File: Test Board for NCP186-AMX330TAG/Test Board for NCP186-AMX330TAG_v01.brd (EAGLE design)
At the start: 11 x 9.3 mm, 7 parts

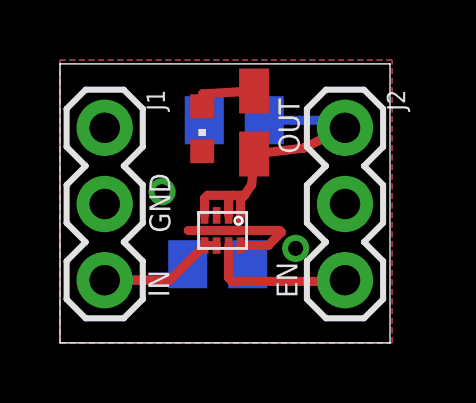
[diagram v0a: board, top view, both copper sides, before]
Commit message: Updated NCP part
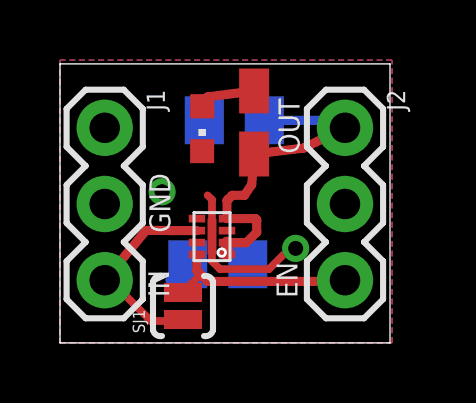
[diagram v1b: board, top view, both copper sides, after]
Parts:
- added SJ1: SOLDERJUMPERNO, SparkFun-Retired:SJ_2S-NO
- moved U$1 1.70 mm to (5.67, 2.74), turned to 90 degrees
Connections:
- net EN: now also J1.3, SJ1.1; no longer J2.3
- net IIN: now also J2.3, SJ1.2; no longer J1.3
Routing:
- net EN: track 5.02 -> 7.05 mm
- net GND: track 4.19 -> 5.43 mm
- net OUT: track 10.8 -> 11.7 mm
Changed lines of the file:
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@@
 <elements>
 <element name="C1" library="resistor" package="C0805K" value="" x="5.81" y="7.42" rot="MR0"/>
-<element name="U$1" library="Ladvien_Eagle_Parts" package="XDFN8" value="NCP186-AMX330TAG" x="6.22" y="4.35" smashed="yes" rot="R180"/>
 <element name="C2" library="resistor" package="C0805K" value="" x="5.26" y="2.62" rot="MR180"/>
 <element name="J1" library="SparkFun-Connectors" package="1X03" value="" x="1.49" y="7.17" rot="R270"/>
@@
 <attribute name="VALUE" x="9.01184375" y="6.71238125" size="1.27" layer="27" rot="R90"/>
 </element>
+<element name="U$1" library="Ladvien_Eagle_Parts" package="XDFN8" value="NCP186-AMX330TAG" x="5.6672625" y="2.7424625" rot="R90"/>
+<element name="SJ1" library="SparkFun-Retired" package="SJ_2S-NO" value="SOLDERJUMPERNO" x="4.1" y="1.23" rot="R90"/>
 </elements>
 <signals>
 <signal name="IIN">
-<contactref element="J1" pad="3"/>
 <contactref element="C2" pad="1"/>
-<contactref element="U$1" pad="8"/>
-<contactref element="U$1" pad="7"/>
-<wire x1="1.49" y1="2.09" x2="3.6625" y2="2.09" width="0.3048" layer="1"/>
-<wire x1="3.6625" y1="2.09" x2="4.82" y2="3.2475" width="0.3048" layer="1"/>
-<wire x1="4.82" y1="3.2475" x2="5.22" y2="3.2475" width="0.3048" layer="1"/>
 <wire x1="4.26" y1="2.62" x2="4.1925" y2="2.62" width="0.3048" layer="16"/>
 <wire x1="4.1925" y1="2.62" x2="3.6625" y2="2.09" width="0.3048" layer="16"/>
-<wire x1="3.6625" y1="2.09" x2="1.49" y2="2.09" width="0.3048" layer="16"/>
+<contactref element="U$1" pad="7" route="any" routetag="G$1.IN"/>
+<contactref element="U$1" pad="8" route="any" routetag="G$1.IN"/>
+<contactref element="J2" pad="3"/>
+<wire x1="4.5647625" y1="2.9424625" x2="4.5647625" y2="2.4052375" width="0.3048" layer="1"/>
+<wire x1="4.5647625" y1="2.4052375" x2="4.68653125" y2="2.28346875" width="0.3048" layer="1"/>
+<wire x1="4.68653125" y1="2.28346875" x2="4.92" y2="2.05" width="0.3048" layer="1"/>
+<wire x1="4.92" y1="2.05" x2="9.46" y2="2.05" width="0.3048" layer="1"/>
+<wire x1="9.46" y1="2.05" x2="9.5" y2="2.09" width="0.4064" layer="1"/>
+<contactref element="SJ1" pad="2"/>
+<wire x1="4.1" y1="1.68" x2="4.1" y2="1.6969375" width="0.254" layer="1"/>
+<wire x1="4.1" y1="1.6969375" x2="4.68653125" y2="2.28346875" width="0.254" layer="1"/>
+<wire x1="4.5647625" y1="2.4052375" x2="4.26" y2="2.62" width="0" layer="19" extent="1-16"/>
 </signal>
 <signal name="GND">
 <contactref element="J1" pad="2"/>
-<contactref element="U$1" pad="PAD"/>
-<contactref element="U$1" pad="5"/>
 <contactref element="C2" pad="2"/>
 <contactref element="C1" pad="2"/>
@@
 <vertex x="11.07" y="9.43"/>
 </polygon>
-<wire x1="5.42" y1="3.75" x2="7.32" y2="3.75" width="0.3048" layer="1"/>
-<wire x1="7.32" y1="3.75" x2="7.38" y2="3.69" width="0.3048" layer="1"/>
-<wire x1="6.02" y1="3.2475" x2="6.9375" y2="3.2475" width="0.3048" layer="1"/>
-<wire x1="6.9375" y1="3.2475" x2="7.38" y2="3.69" width="0.3048" layer="1"/>
 <via x="3.402915625" y="5.03813125" extent="1-16" drill="0.5"/>
 <via x="7.855496875" y="3.1503875" extent="1-16" drill="0.5"/>
-<wire x1="4.935915625" y1="3.745275" x2="4.27164375" y2="3.745275" width="0.3048" layer="1"/>
+<contactref element="U$1" pad="PAD"/>
+<contactref element="U$1" pad="5"/>
+<wire x1="5.0672625" y1="3.5424625" x2="5.0672625" y2="4.7727375" width="0.254" layer="1"/>
+<wire x1="5.0672625" y1="4.7727375" x2="4.92" y2="4.92" width="0.254" layer="1"/>
+<wire x1="5.0672625" y1="3.5424625" x2="5.0672625" y2="2.7227375" width="0.254" layer="1"/>
+<wire x1="5.0672625" y1="2.7227375" x2="5.33" y2="2.46" width="0.254" layer="1"/>
+<wire x1="5.33" y1="2.46" x2="6.97" y2="2.46" width="0.254" layer="1"/>
+<wire x1="6.97" y1="2.46" x2="7.79" y2="3.28" width="0.254" layer="1"/>
+<wire x1="5.0672625" y1="3.5424625" x2="4.5647625" y2="4.1424625" width="0" layer="19" extent="1-1"/>
 </signal>
 <signal name="OUT">
-<contactref element="U$1" pad="4"/>
-<contactref element="U$1" pad="1"/>
-<contactref element="U$1" pad="2"/>
 <contactref element="J2" pad="1"/>
 <contactref element="C1" pad="1"/>
@@
 <wire x1="6.39215" y1="5.280259375" x2="6.15" y2="4.92" width="0.3048" layer="1"/>
 <wire x1="6.15" y1="4.92" x2="5.74" y2="4.92" width="0.3048" layer="1"/>
-<wire x1="5.74" y1="4.92" x2="4.92" y2="4.92" width="0.3048" layer="1"/>
-<wire x1="4.82" y1="4.25" x2="4.82" y2="4.82" width="0.3048" layer="1"/>
-<wire x1="4.82" y1="4.82" x2="4.92" y2="4.92" width="0.3048" layer="1"/>
-<wire x1="5.62" y1="4.25" x2="5.62" y2="4.8" width="0.3048" layer="1"/>
 <wire x1="5.62" y1="4.8" x2="5.74" y2="4.92" width="0.3048" layer="1"/>
-<wire x1="6.02" y1="4.25" x2="6.02" y2="4.79" width="0.3048" layer="1"/>
-<wire x1="6.02" y1="4.79" x2="6.15" y2="4.92" width="0.3048" layer="1"/>
 <wire x1="6.81" y1="7.42" x2="9.25" y2="7.42" width="0.3048" layer="16"/>
 <wire x1="9.25" y1="7.42" x2="9.5" y2="7.17" width="0.3048" layer="16"/>
+<contactref element="U$1" pad="4"/>
+<contactref element="U$1" pad="1"/>
+<contactref element="U$1" pad="2"/>
+<wire x1="5.5672625" y1="2.9424625" x2="5.5672625" y2="3.3424625" width="0.4064" layer="1"/>
+<wire x1="5.5672625" y1="3.3424625" x2="6.2124625" y2="3.3424625" width="0.3048" layer="1"/>
+<wire x1="6.2124625" y1="3.3424625" x2="6.56" y2="3.69" width="0.3048" layer="1"/>
+<wire x1="5.5672625" y1="4.1424625" x2="6.5175375" y2="4.1424625" width="0.3048" layer="1"/>
+<wire x1="6.5175375" y1="4.1424625" x2="6.56" y2="4.1" width="0.3048" layer="1"/>
+<wire x1="6.56" y1="4.1" x2="6.56" y2="3.69" width="0.3048" layer="1"/>
+<wire x1="5.5672625" y1="4.1424625" x2="5.5672625" y2="4.7472625" width="0.3048" layer="1"/>
+<wire x1="5.5672625" y1="4.7472625" x2="5.62" y2="4.8" width="0.3048" layer="1"/>
 </signal>
 <signal name="EN">
 <contactref element="U$1" pad="6"/>
-<contactref element="J2" pad="3"/>
-<wire x1="5.62" y1="3.2475" x2="5.62" y2="2.17" width="0.3048" layer="1"/>
-<wire x1="5.62" y1="2.17" x2="5.74" y2="2.05" width="0.3048" layer="1"/>
-<wire x1="5.74" y1="2.05" x2="9.46" y2="2.05" width="0.3048" layer="1"/>
-<wire x1="9.46" y1="2.05" x2="9.5" y2="2.09" width="0.3048" layer="1"/>
+<contactref element="J1" pad="3"/>
+<wire x1="4.5647625" y1="3.7424625" x2="3.7424625" y2="3.7424625" width="0.3048" layer="1"/>
+<wire x1="3.7424625" y1="3.7424625" x2="3.46725625" y2="3.74861875" width="0.3048" layer="1"/>
+<wire x1="3.46725625" y1="3.74861875" x2="2.86725625" y2="3.74861875" width="0.3048" layer="1"/>
+<wire x1="2.86725625" y1="3.74861875" x2="1.49" y2="2.09" width="0.3048" layer="1"/>
+<contactref element="SJ1" pad="1"/>
+<wire x1="1.49" y1="2.09" x2="1.672553125" y2="2.09" width="0.254" layer="1"/>
+<wire x1="1.672553125" y1="2.09" x2="3.032228125" y2="0.730325" width="0.254" layer="1"/>
+<wire x1="3.032228125" y1="0.730325" x2="4.050325" y2="0.730325" width="0.254" layer="1"/>
+<wire x1="4.050325" y1="0.730325" x2="4.1" y2="0.78" width="0.254" layer="1"/>
 </signal>
 <signal name="N$1">
 <contactref element="R1" pad="2"/>
 <contactref element="LED1" pad="A"/>
-<wire x1="6.47184375" y1="8.39988125" x2="4.75124375" y2="8.298875" width="0.3048" layer="1"/>
-<wire x1="4.75124375" y1="8.298875" x2="4.74" y2="7.89" width="0.3048" layer="1"/>
+<wire x1="6.47184375" y1="8.39988125" x2="4.92" y2="8.2" width="0.3048" layer="1"/>
+<wire x1="4.92" y1="8.2" x2="4.74" y2="7.89" width="0.3048" layer="1"/>
 </signal>
 </signals>
